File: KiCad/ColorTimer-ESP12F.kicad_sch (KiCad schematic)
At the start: 1 part, among them U1 ESP-12F

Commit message: 回路図ひき始め
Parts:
- added J1: SERIAL CON, symbol Connector_Generic:Conn_01x06
- added R1, R2, R3, R4, R5, R6: 10k, symbol Device:R_Small_US
- added SW1: RESET, symbol Switch:SW_Push
- added SW2: FLASH, symbol Switch:SW_Push
- added SW3: TOROGGER, symbol Switch:SW_Push
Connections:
- net at U1.1 (REST): now also R1.2, SW1.2
- net at U1.10 (GPIO15): now also R3.1
- net at U1.11 (GPIO2): now also R4.2
- net at U1.12 (GPIO0): now also R5.2, SW2.1
- net at U1.15 (RXD): now also J1.4 (Pin_4)
- net at U1.16 (TXD): now also J1.5 (Pin_5)
- net at U1.3 (CH_PD): now also R2.2
- net +3.3V: now reaches U1.8 (VCC)
- net +3.3V: now also J1.3 (Pin_3), R1.1, R2.1, R4.1, R5.1, R6.1
- net GND: now reaches U1.9 (GND)
- net GND: now also J1.1 (Pin_1), R3.2, SW1.1, SW2.2, SW3.1
- new net: J1.2 (Pin_2), J1.6 (Pin_6)
- new net: R6.2, SW3.2
- no-connect marks 0 -> 9
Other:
- note added: "+3.3V"
- note added: "CTS"
- note added: "GND"
- note added: "RTS"
- note added: "RxD"
- note added: "TxD"
- moved on the sheet: U1

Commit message: 回路図、パターン暫定版
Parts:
- added C1: 100u, Capacitor_THT:CP_Radial_D5.0mm_P2.50mm, symbol Device:C_Polarized
- added C2, C3: 0.1u, Capacitor_THT:C_Disc_D3.0mm_W1.6mm_P2.50mm, symbol Device:C_Small
- added C4: 10u, Capacitor_THT:CP_Radial_D5.0mm_P2.50mm, symbol Device:C_Polarized
- added D1: RED LED, LED_THT:LED_D3.0mm, symbol Device:LED_Small_Filled
- added D2: BLUE LED, LED_THT:LED_D3.0mm, symbol Device:LED_Small_Filled
- added H1, H2, H3, H4: MountingHole, MountingHole:MountingHole_3.2mm_M3, symbol Mechanical:MountingHole
- added J2: GPIO_CON, Connector_PinSocket_2.54mm:PinSocket_1x09_P2.54mm_Vertical, symbol Connector_Generic:Conn_01x09
- added J3: Barrel_Jack_Switch, Connector_BarrelJack:BarrelJack_Horizontal, symbol Connector:Barrel_Jack_Switch
- added J4: RED_CON, Connector_PinSocket_2.54mm:PinSocket_1x02_P2.54mm_Vertical, symbol Connector_Generic:Conn_01x02
- added J5: BLUE_CON, Connector_PinSocket_2.54mm:PinSocket_1x02_P2.54mm_Vertical, symbol Connector_Generic:Conn_01x02
- added J6: SW_CON, Connector_PinSocket_2.54mm:PinSocket_1x02_P2.54mm_Vertical, symbol Connector_Generic:Conn_01x02
- added JP1: Power JP, Connector_PinHeader_2.54mm:PinHeader_1x02_P2.54mm_Vertical, symbol Jumper:Jumper_2_Open
- added R7, R8: 330, Resistor_THT:R_Axial_DIN0207_L6.3mm_D2.5mm_P10.16mm_Horizontal, symbol Device:R_Small_US
- added SW4: POWER_SW, Connector_PinHeader_2.54mm:PinHeader_1x03_P2.54mm_Vertical, symbol Switch:SW_SPST
- added U2: L78L33_TO92, Package_TO_SOT_THT:TO-92_Inline_Wide, symbol Regulator_Linear:L78L33_TO92
- J1: footprint (none) -> Connector_PinHeader_2.54mm:PinHeader_1x06_P2.54mm_Horizontal
- R1, R2, R3, R4, R5, R6: footprint (none) -> Resistor_THT:R_Axial_DIN0207_L6.3mm_D2.5mm_P10.16mm_Horizontal
- SW1, SW2: footprint (none) -> Button_Switch_THT:SW_PUSH_6mm_H8mm
- SW3: value TOROGGER -> Trigger SW; footprint (none) -> Button_Switch_THT:SW_PUSH_6mm_H8mm
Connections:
- net +3.3V: now also C3.1, C4.1, J2.8 (Pin_8), JP1.1 (A), U2.1 (VO); no longer J1.3 (Pin_3)
- net GND: now also C1.2, C2.2, C3.2, C4.2, D1.1 (K), D2.1 (K), J2.9 (Pin_9), J3.2, J3.3, J4.2 (Pin_2), J5.2 (Pin_2), J6.2 (Pin_2), U2.2 (GND)
- net GPIO4: now reaches U1.13 (GPIO4)
- net GPIO4: now also J2.1 (Pin_1)
- net GPIO5: now reaches U1.14 (GPIO5)
- net GPIO5: now also J2.2 (Pin_2)
- net ADC: now reaches U1.2 (ADC)
- net ADC: now also J2.7 (Pin_7)
- net GPIO16: now reaches U1.4 (GPIO16)
- net GPIO16: now also R6.2, SW3.2, J2.6 (Pin_6), J6.1 (Pin_1)
- net GPIO14: now reaches U1.5 (GPIO14)
- net GPIO14: now also J2.5 (Pin_5), R7.2
- net GPIO12: now reaches U1.6 (GPIO12)
- net GPIO12: now also J2.3 (Pin_3)
- net GPIO13: now reaches U1.7 (GPIO13)
- net GPIO13: now also J2.4 (Pin_4), R8.2
- new net: J1.3 (Pin_3), JP1.2 (B)
- new net: C1.1, C2.1, SW4.2 (B), U2.3 (VI)
- new net: D1.2 (A), J4.1 (Pin_1), R7.1
- new net: D2.2 (A), J5.1 (Pin_1), R8.1
- new net: J3.1, SW4.1 (A)
- no-connect marks 9 -> 6
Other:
- moved on the sheet: J1, R1, R2, R3, R4, R5, R6, SW1, SW2, SW3, U1

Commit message: 自動書き込み回路追加
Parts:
- removed C1: 100u, Capacitor_THT:CP_Radial_D5.0mm_P2.50mm, symbol Device:C_Polarized
- removed J3: Barrel_Jack_Switch, Connector_BarrelJack:BarrelJack_Horizontal, symbol Connector:Barrel_Jack_Switch
- removed JP1: Power JP, Connector_PinHeader_2.54mm:PinHeader_1x02_P2.54mm_Vertical, symbol Jumper:Jumper_2_Open
- added C5, C6: 0.1u, Capacitor_THT:C_Disc_D3.0mm_W1.6mm_P2.50mm, symbol Device:C_Small
- added Q1, Q2: 2N7000, Package_TO_SOT_THT:TO-92_Inline, symbol Transistor_FET:2N7000
- J1: value SERIAL CON -> FTDI SERIAL
- R7, R8: value 330 -> 470
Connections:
- net GND: now also C5.2, C6.2
- net at J1.2 (Pin_2): now also Q1.1 (S), Q2.2 (G); no longer J1.6 (Pin_6)
- net at J1.3 (Pin_3): now also SW4.2 (B)
- net +5V: now reaches C2.1, U2.3 (VI)
- net +5V: now also SW4.1 (A); no longer SW4.2 (B)
- net EN: now reaches R2.2, U1.3 (CH_PD)
- net EN: now also C6.1, Q1.3 (D)
- net GPIO0: now reaches R5.2, SW2.1, U1.12 (GPIO0)
- net GPIO0: now also Q2.3 (D)
- net at R1.2, SW1.2, U1.1 (REST): now also C5.1
- new net: J1.6 (Pin_6), Q1.2 (G), Q2.1 (S)
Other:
- note added: "DTR"
- note added: "VCC"
- note removed: "+3.3V"
- note removed: "CTS"
- moved on the sheet: J1, R1, SW1, SW4

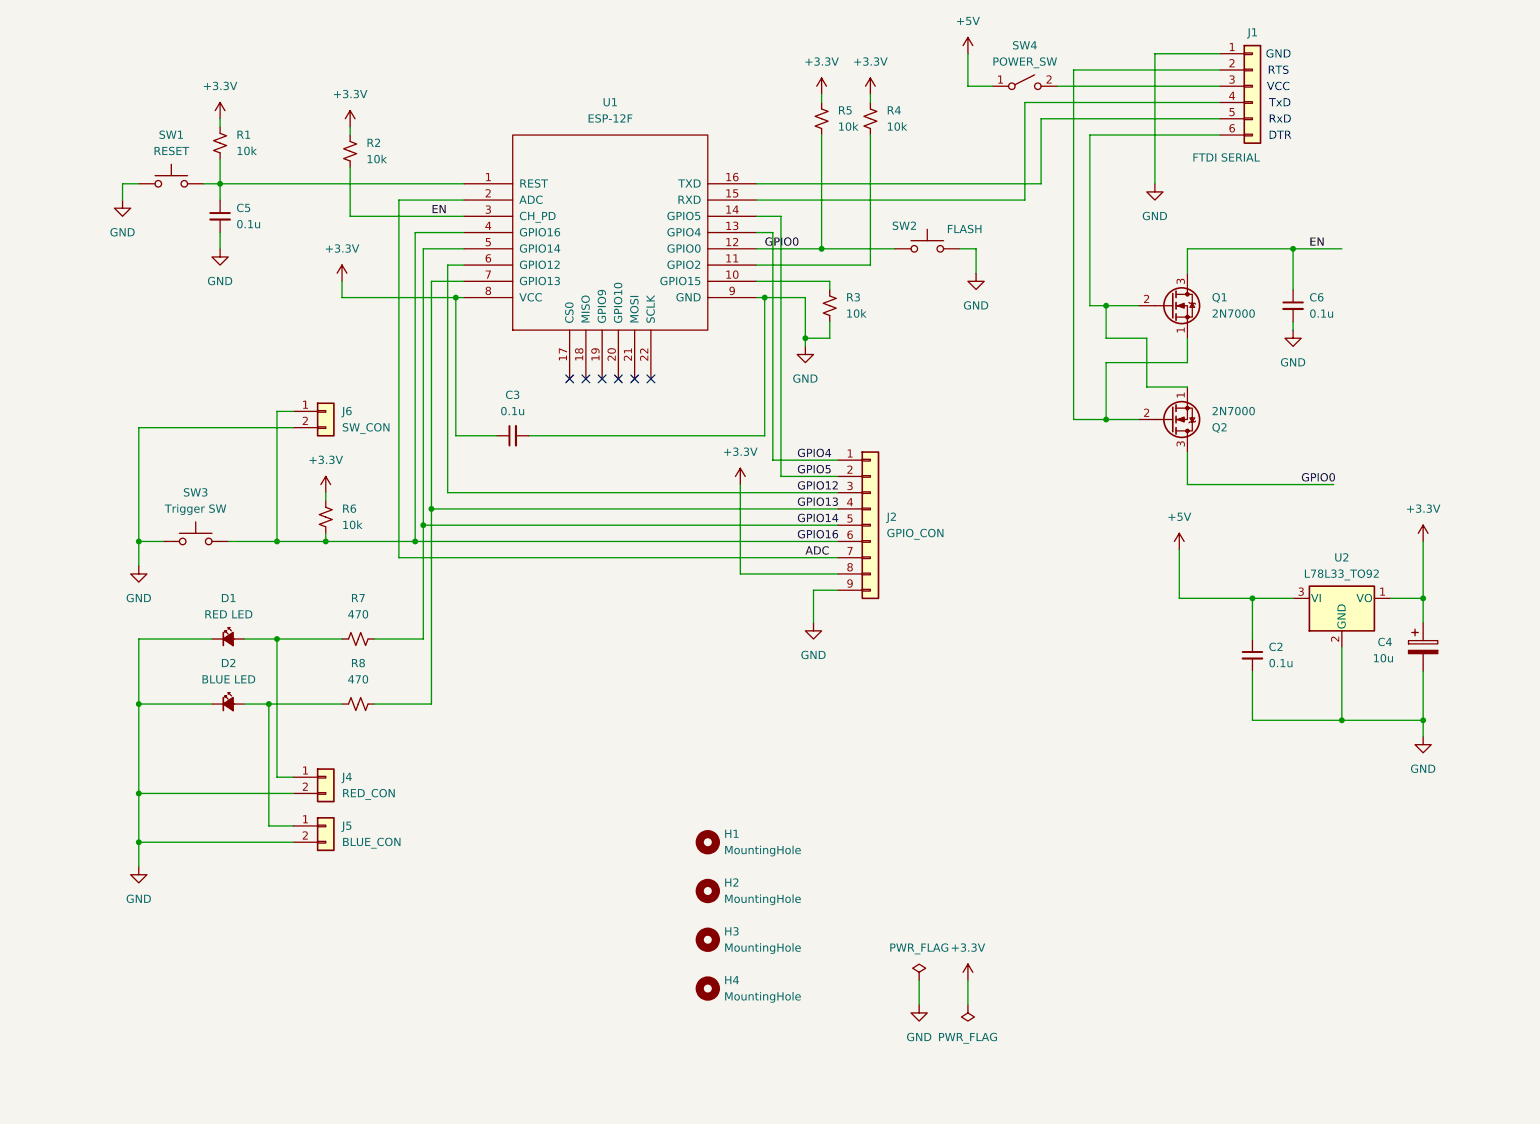
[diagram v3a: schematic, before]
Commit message: CH340K USBシリアル追加
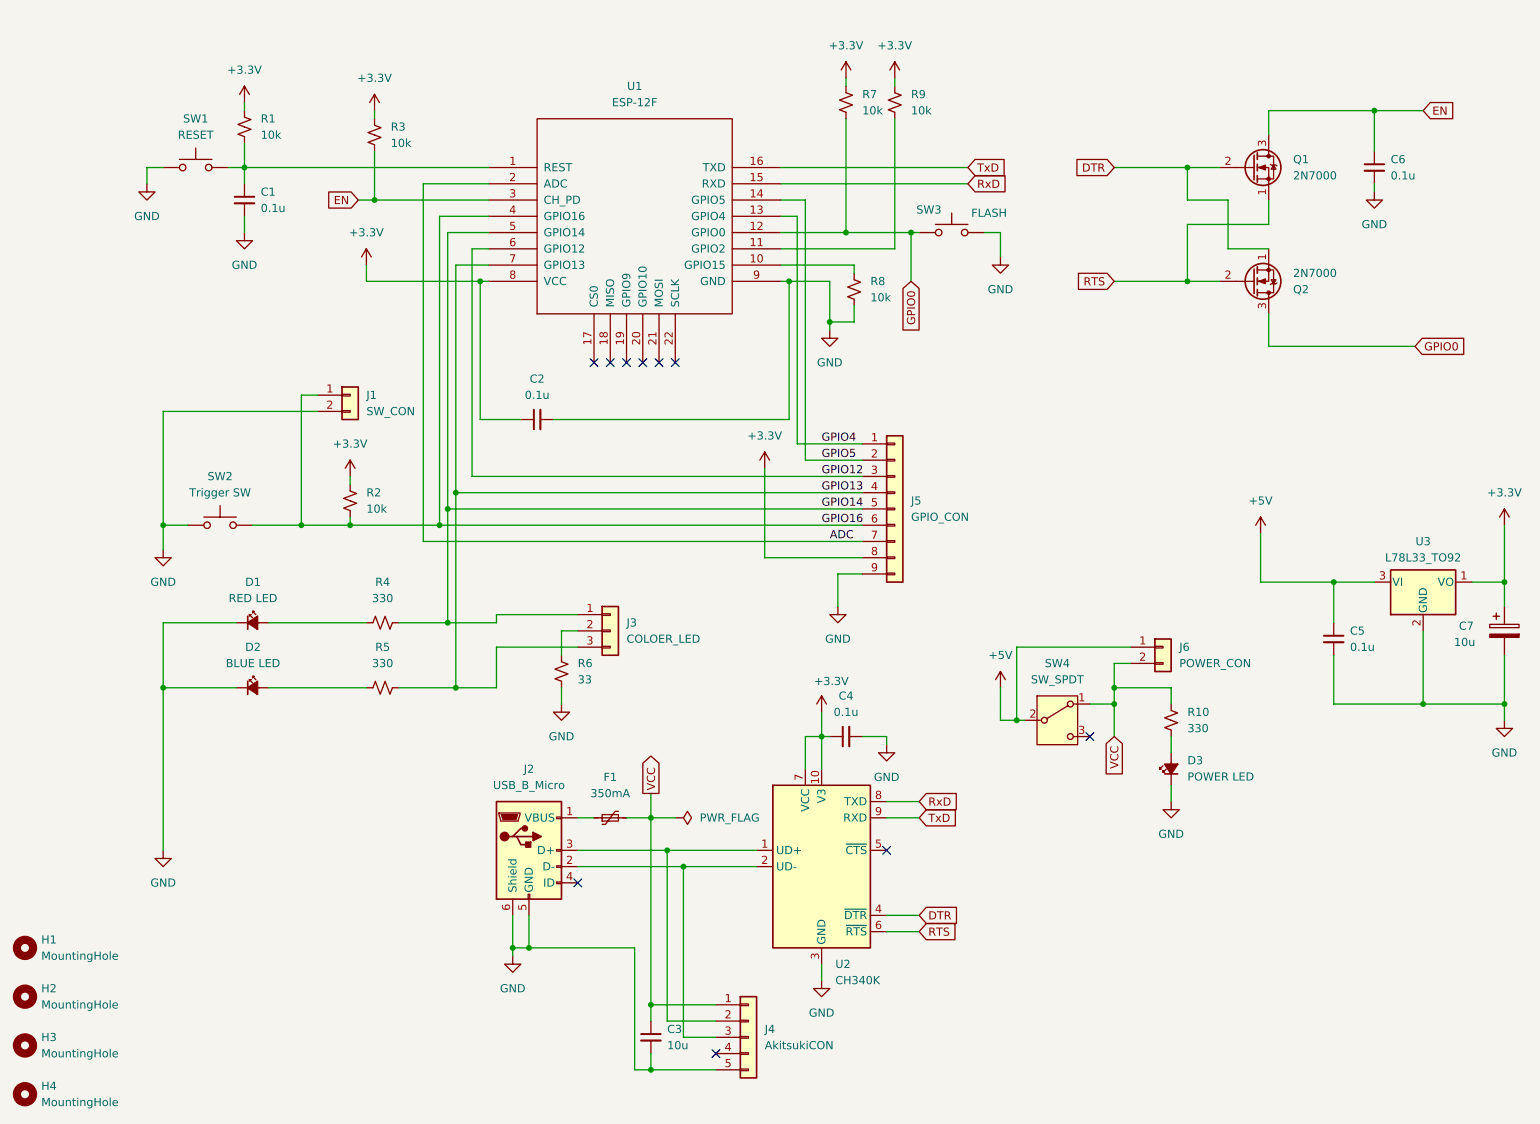
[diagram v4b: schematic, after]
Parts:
- removed J1: FTDI SERIAL, Connector_PinHeader_2.54mm:PinHeader_1x06_P2.54mm_Horizontal, symbol Connector_Generic:Conn_01x06
- removed J4: RED_CON, Connector_PinSocket_2.54mm:PinSocket_1x02_P2.54mm_Vertical, symbol Connector_Generic:Conn_01x02
- removed J5: BLUE_CON, Connector_PinSocket_2.54mm:PinSocket_1x02_P2.54mm_Vertical, symbol Connector_Generic:Conn_01x02
- removed SW4: POWER_SW, Connector_PinHeader_2.54mm:PinHeader_1x03_P2.54mm_Vertical, symbol Switch:SW_SPST
- added C3: 10u, Capacitor_THT:C_Disc_D3.0mm_W1.6mm_P2.50mm, symbol Device:C_Small
- added C4: 0.1u, Capacitor_THT:C_Disc_D3.0mm_W1.6mm_P2.50mm, symbol Device:C_Small
- added D3: POWER LED, LED_THT:LED_D3.0mm, symbol Device:LED_Small_Filled
- added F1: 350mA, symbol Device:Polyfuse_Small
- added J2: USB_B_Micro, symbol Connector:USB_B_Micro
- added J3: COLOER_LED, symbol Connector_Generic:Conn_01x03
- added J4: AkitsukiCON, symbol Connector_Generic:Conn_01x05
- added J6: POWER_CON, Connector_PinSocket_2.54mm:PinSocket_1x02_P2.54mm_Vertical, symbol Connector_Generic:Conn_01x02
- added R10: 330, Resistor_THT:R_Axial_DIN0207_L6.3mm_D2.5mm_P10.16mm_Horizontal, symbol Device:R_Small_US
- added R6: 33, Resistor_THT:R_Axial_DIN0207_L6.3mm_D2.5mm_P10.16mm_Horizontal, symbol Device:R_Small_US
- added SW4: SW_SPDT, symbol Switch:SW_SPDT
- added U2: CH340K, Package_SO:SSOP-10-1EP_3.9x4.9mm_P1mm_EP2.1x3.3mm, symbol Interface_USB:CH340K
- R4: renamed from R7; value 470 -> 330
- R5: renamed from R8; value 470 -> 330
- renumbered C5 to C1, C3 to C2, C2 to C5, C4 to C7, J6 to J1, J2 to J5, R6 to R2, R2 to R3, R5 to R7, R3 to R8, R4 to R9, SW3 to SW2, SW2 to SW3, U2 to U3
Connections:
- net +3.3V: now also C4.1, U2.10 (V3), U2.7 (VCC)
- net +5V: now also J6.1 (Pin_1), SW4.2 (B)
- net GND: now also C3.2, C4.2, D3.1 (K), J2.5 (GND), J2.6 (Shield), J4.5 (Pin_5), R6.1, U2.11 (GND), U2.3 (GND)
- net GPIO13: now also J3.3 (Pin_3)
- net GPIO14: now also J3.1 (Pin_1)
- net RTS: now reaches Q1.1 (S), Q2.2 (G)
- net RTS: now also U2.6 (~{RTS})
- net RxD: now reaches U1.15 (RXD)
- net RxD: now also U2.8 (TXD)
- net TxD: now reaches U1.16 (TXD)
- net TxD: now also U2.9 (RXD)
- net DTR: now reaches Q1.2 (G), Q2.1 (S)
- net DTR: now also U2.4 (~{DTR})
- new net: J3.2 (Pin_2), R6.2
- new net: F1.1, J2.1 (VBUS)
- new net: J2.3 (D+), J4.2 (Pin_2), U2.1 (UD+)
- new net: J2.2 (D-), J4.3 (Pin_3), U2.2 (UD-)
- new net: D3.2 (A), R10.1
- new net VCC: C3.1, F1.2, J4.1 (Pin_1), J6.2 (Pin_2), R10.2, SW4.1 (A)
- no-connect marks 6 -> 10
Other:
- note removed: "DTR"
- note removed: "GND"
- note removed: "RTS"
- note removed: "RxD"
- note removed: "TxD"
- note removed: "VCC"
- moved on the sheet: C1, C2, C5, C6, C7, D1, D2, H1, H2, H3, H4, J1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

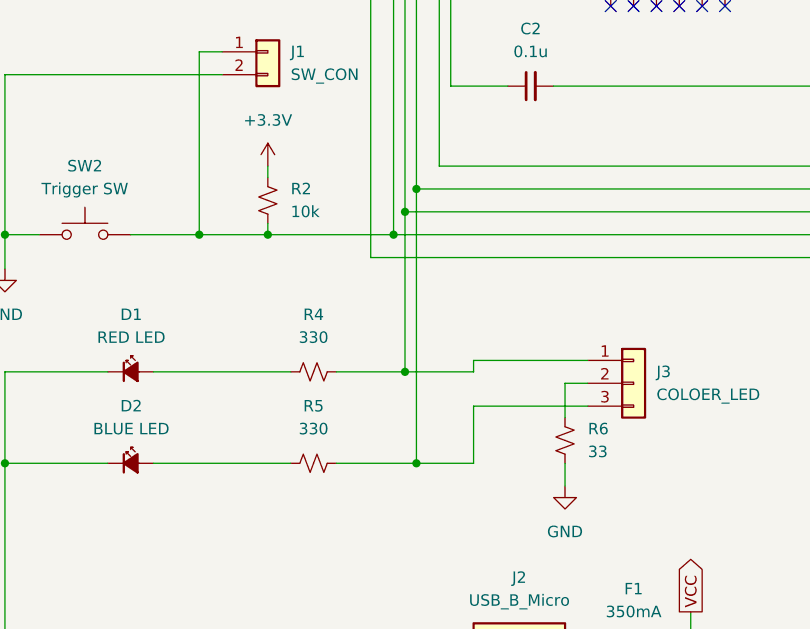
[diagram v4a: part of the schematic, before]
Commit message: LED配線変更
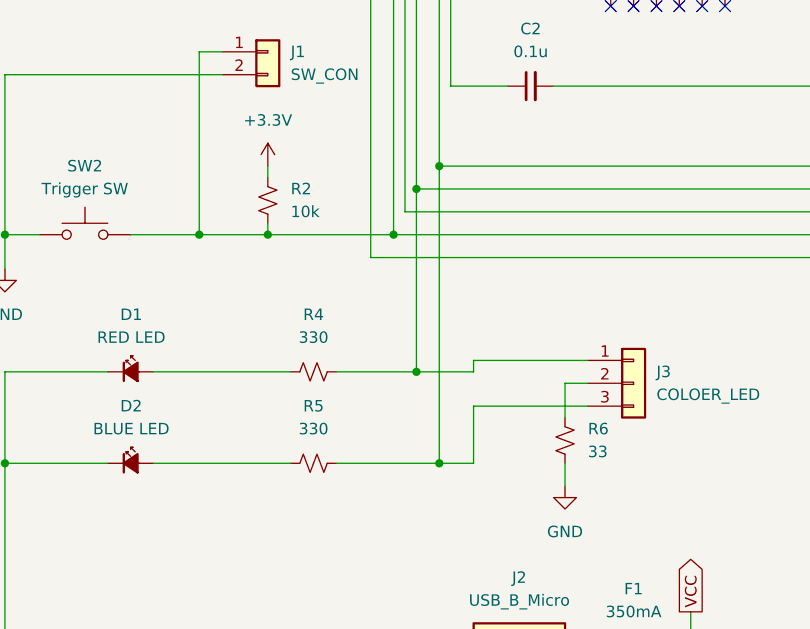
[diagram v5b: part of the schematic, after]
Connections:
- net GPIO12: now also J3.3 (Pin_3), R5.2
- net GPIO13: now also J3.1 (Pin_1), R4.2; no longer J3.3 (Pin_3), R5.2
- net GPIO14: no longer J3.1 (Pin_1), R4.2
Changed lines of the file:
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@@
 	)
 	(junction
-		(at 87.63 118.11)
+		(at 91.44 95.25)
 		(diameter 0)
 		(color 0 0 0 0)
@@
 	)
 	(junction
-		(at 88.9 128.27)
-		(diameter 0)
-		(color 0 0 0 0)
-	)
-	(junction
 		(at 92.71 64.77)
 		(diameter 0)
@@
 	)
 	(junction
+		(at 252.73 111.76)
+		(diameter 0)
+		(color 0 0 0 0)
+	)
+	(junction
+		(at 119.38 187.96)
+		(diameter 0)
+		(color 0 0 0 0)
+	)
+	(junction
+		(at 147.32 71.12)
+		(diameter 0)
+		(color 0 0 0 0)
+	)
+	(junction
+		(at 88.9 118.11)
+		(diameter 0)
+		(color 0 0 0 0)
+	)
+	(junction
+		(at 91.44 128.27)
+		(diameter 0)
+		(color 0 0 0 0)
+	)
+	(junction
+		(at 203.2 64.77)
+		(diameter 0)
+		(color 0 0 0 0)
+	)
+	(junction
+		(at 191.77 128.27)
+		(diameter 0)
+		(color 0 0 0 0)
+	)
+	(junction
+		(at 121.92 153.67)
+		(diameter 0)
+		(color 0 0 0 0)
+	)
+	(junction
+		(at 119.38 148.59)
+		(diameter 0)
+		(color 0 0 0 0)
+	)
+	(junction
+		(at 176.53 133.35)
+		(diameter 0)
+		(color 0 0 0 0)
+	)
+	(junction
+		(at 43.18 128.27)
+		(diameter 0)
+		(color 0 0 0 0)
+	)
+	(junction
+		(at 160.02 57.15)
+		(diameter 0)
+		(color 0 0 0 0)
+	)
+	(junction
+		(at 252.73 130.81)
+		(diameter 0)
+		(color 0 0 0 0)
+	)
+	(junction
+		(at 86.36 102.87)
+		(diameter 0)
+		(color 0 0 0 0)
+	)
+	(junction
+		(at 140.97 64.77)
+		(diameter 0)
+		(color 0 0 0 0)
+	)
+	(junction
+		(at 55.88 46.99)
+		(diameter 0)
+		(color 0 0 0 0)
+	)
+	(junction
+		(at 72.39 102.87)
+		(diameter 0)
+		(color 0 0 0 0)
+	)
+	(junction
 		(at 88.9 97.79)
 		(diameter 0)
@@
 	)
 	(junction
-		(at 252.73 111.76)
-		(diameter 0)
-		(color 0 0 0 0)
-	)
-	(junction
-		(at 119.38 187.96)
-		(diameter 0)
-		(color 0 0 0 0)
-	)
-	(junction
-		(at 147.32 71.12)
-		(diameter 0)
-		(color 0 0 0 0)
-	)
-	(junction
-		(at 203.2 64.77)
-		(diameter 0)
-		(color 0 0 0 0)
-	)
-	(junction
-		(at 191.77 128.27)
-		(diameter 0)
-		(color 0 0 0 0)
-	)
-	(junction
-		(at 121.92 153.67)
-		(diameter 0)
-		(color 0 0 0 0)
-	)
-	(junction
-		(at 119.38 148.59)
-		(diameter 0)
-		(color 0 0 0 0)
-	)
-	(junction
-		(at 176.53 133.35)
-		(diameter 0)
-		(color 0 0 0 0)
-	)
-	(junction
-		(at 43.18 128.27)
-		(diameter 0)
-		(color 0 0 0 0)
-	)
-	(junction
-		(at 160.02 57.15)
-		(diameter 0)
-		(color 0 0 0 0)
-	)
-	(junction
-		(at 252.73 130.81)
-		(diameter 0)
-		(color 0 0 0 0)
-	)
-	(junction
-		(at 86.36 102.87)
-		(diameter 0)
-		(color 0 0 0 0)
-	)
-	(junction
-		(at 140.97 64.77)
-		(diameter 0)
-		(color 0 0 0 0)
-	)
-	(junction
-		(at 55.88 46.99)
-		(diameter 0)
-		(color 0 0 0 0)
-	)
-	(junction
-		(at 72.39 102.87)
-		(diameter 0)
-		(color 0 0 0 0)
-	)
-	(junction
 		(at 191.77 130.81)
 		(diameter 0)
@@
 	(junction
 		(at 232.41 38.1)
-		(diameter 0)
-		(color 0 0 0 0)
-	)
-	(junction
-		(at 87.63 100.33)
 		(diameter 0)
 		(color 0 0 0 0)
@@
 	(wire
 		(pts
-			(xy 87.63 118.11) (xy 80.01 118.11)
+			(xy 88.9 97.79) (xy 88.9 118.11)
 		)
 		(stroke
@@
 	(wire
 		(pts
+			(xy 91.44 95.25) (xy 91.44 128.27)
+		)
+		(stroke
+			(width 0)
+			(type default)
+		)
+	)
+	(wire
+		(pts
 			(xy 124.46 156.21) (xy 124.46 182.88)
 		)
@@
 	(wire
 		(pts
-			(xy 87.63 100.33) (xy 87.63 118.11)
-		)
-		(stroke
-			(width 0)
-			(type default)
-		)
-	)
-	(wire
-		(pts
 			(xy 83.82 49.53) (xy 83.82 105.41)
 		)
@@
 	(wire
 		(pts
-			(xy 88.9 97.79) (xy 88.9 128.27)
-		)
-		(stroke
-			(width 0)
-			(type default)
-		)
-	)
-	(wire
-		(pts
 			(xy 140.97 64.77) (xy 147.32 64.77)
 		)
@@
 	(wire
 		(pts
-			(xy 88.9 128.27) (xy 95.25 128.27)
-		)
-		(stroke
-			(width 0)
-			(type default)
-		)
-	)
-	(wire
-		(pts
 			(xy 226.06 123.19) (xy 226.06 130.81)
 		)
@@
 	(wire
 		(pts
-			(xy 88.9 128.27) (xy 80.01 128.27)
+			(xy 80.01 128.27) (xy 91.44 128.27)
 		)
 		(stroke
@@
 	(wire
 		(pts
-			(xy 87.63 118.11) (xy 95.25 118.11)
+			(xy 80.01 118.11) (xy 88.9 118.11)
 		)
 		(stroke
@@
 	(wire
 		(pts
+			(xy 88.9 118.11) (xy 95.25 118.11)
+		)
+		(stroke
+			(width 0)
+			(type default)
+		)
+	)
+	(wire
+		(pts
 			(xy 105.41 128.27) (xy 105.41 130.81)
 		)
@@
 		)
 		(stroke
+			(width 0)
+			(type default)
+		)
+	)
+	(wire
+		(pts
+			(xy 91.44 128.27) (xy 95.25 128.27)
+		)
+		(stroke

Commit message: 部品の関連付けなど
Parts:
- F1: footprint (none) -> Fuse:Fuse_1206_3216Metric_Pad1.42x1.75mm_HandSolder
- J2: footprint (none) -> Connector_USB:USB_Micro-B_Molex-105017-0001
- J3, SW4: footprint (none) -> Connector_PinSocket_2.54mm:PinSocket_1x03_P2.54mm_Vertical
- J4: footprint (none) -> Connector_PinSocket_2.54mm:PinSocket_1x05_P2.54mm_Vertical
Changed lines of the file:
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@@
 			)
 		)
-		(property "Footprint" ""
+		(property "Footprint" "Connector_PinSocket_2.54mm:PinSocket_1x03_P2.54mm_Vertical"
 			(at 113.03 119.38 0)
 			(effects
@@
 			)
 		)
-		(property "Footprint" ""
+		(property "Footprint" "Fuse:Fuse_1206_3216Metric_Pad1.42x1.75mm_HandSolder"
 			(at 118.11 147.32 0)
 			(effects
@@
 			)
 		)
-		(property "Footprint" ""
+		(property "Footprint" "Connector_PinSocket_2.54mm:PinSocket_1x05_P2.54mm_Vertical"
 			(at 134.62 182.88 0)
 			(effects
@@
 			)
 		)
-		(property "Footprint" ""
+		(property "Footprint" "Connector_USB:USB_Micro-B_Molex-105017-0001"
 			(at 104.14 154.94 0)
 			(effects
@@
 			)
 		)
-		(property "Footprint" ""
+		(property "Footprint" "Connector_PinSocket_2.54mm:PinSocket_1x03_P2.54mm_Vertical"
 			(at 182.88 133.35 0)
 			(effects
